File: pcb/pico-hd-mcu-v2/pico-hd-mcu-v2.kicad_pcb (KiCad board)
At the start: 2 copper layers, 87.9 x 88 mm, 43 parts

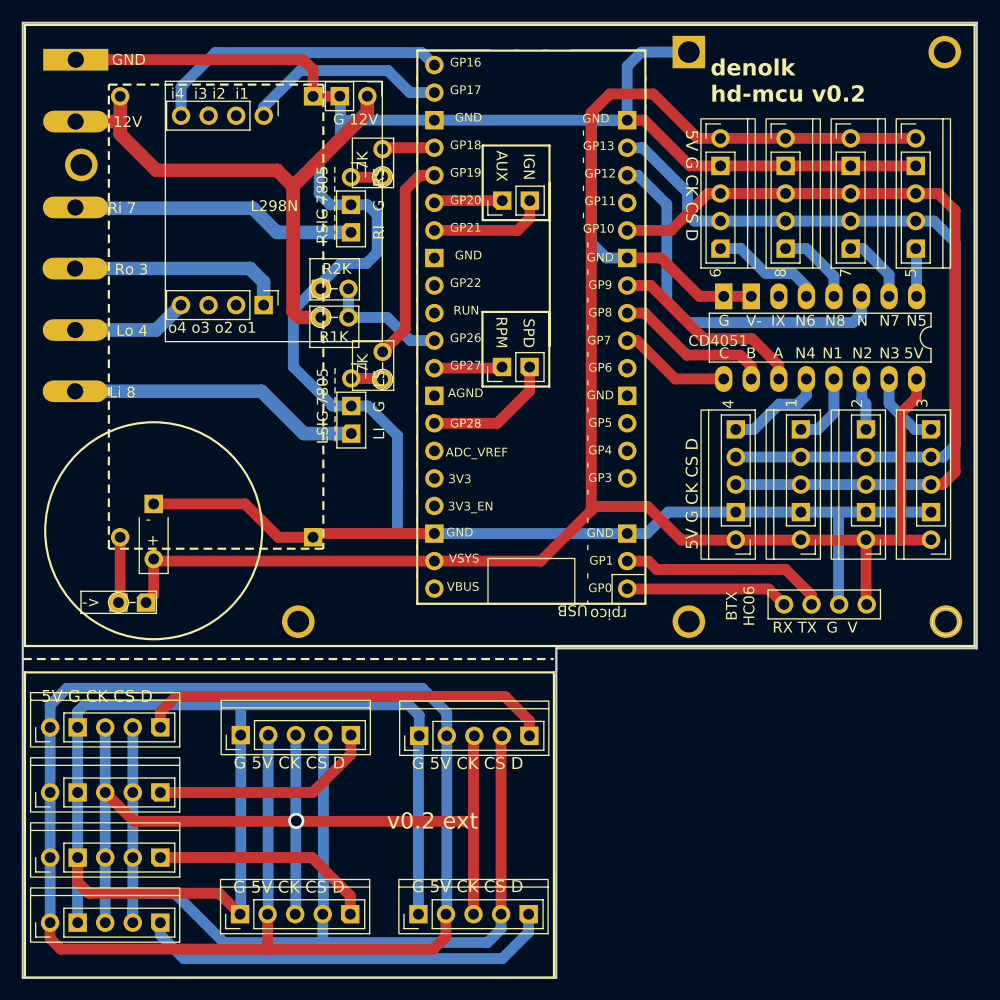
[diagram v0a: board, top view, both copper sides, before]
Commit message: update pcb - ext mosfet switch
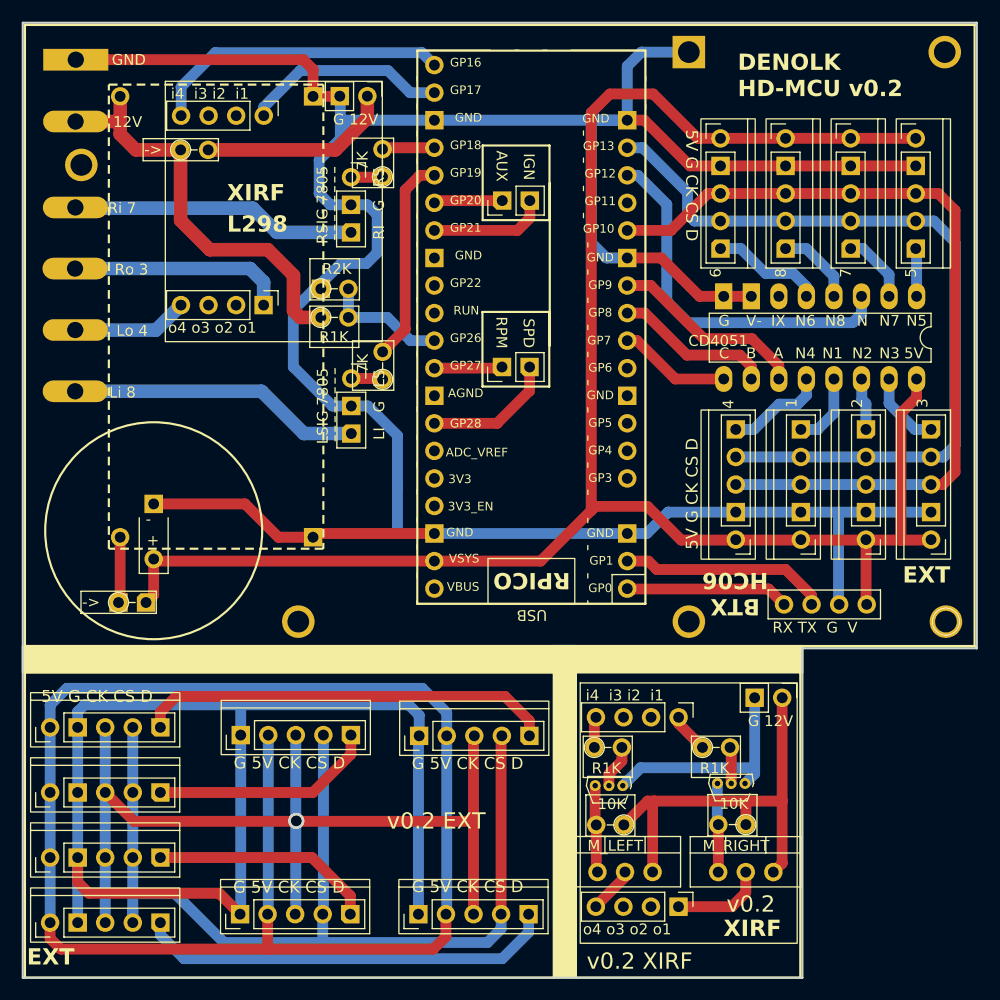
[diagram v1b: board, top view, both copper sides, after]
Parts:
- added ->: R_Axial_DIN0204_L3.6mm_D1.6mm_P2.54mm_Vertical, Resistor_THT:R_Axial_DIN0204_L3.6mm_D1.6mm_P2.54mm_Vertical, F.Cu at (36.4, 38.3)
- added 10K: R_Axial_DIN0204_L3.6mm_D1.6mm_P2.54mm_Vertical, Resistor_THT:R_Axial_DIN0204_L3.6mm_D1.6mm_P2.54mm_Vertical, F.Cu at (77.2, 100.5)
- added 10K: R_Axial_DIN0204_L3.6mm_D1.6mm_P2.54mm_Vertical, Resistor_THT:R_Axial_DIN0204_L3.6mm_D1.6mm_P2.54mm_Vertical, F.Cu at (88.5, 100.5)
- added R1K: R_Axial_DIN0204_L3.6mm_D1.6mm_P2.54mm_Vertical, Resistor_THT:R_Axial_DIN0204_L3.6mm_D1.6mm_P2.54mm_Vertical, F.Cu at (74.5, 93.4)
- added R1K: R_Axial_DIN0204_L3.6mm_D1.6mm_P2.54mm_Vertical, Resistor_THT:R_Axial_DIN0204_L3.6mm_D1.6mm_P2.54mm_Vertical, F.Cu at (84.5, 93.4)
- added REF**: 22RG, Package_TO_SOT_THT:TO-92S, F.Cu at (88.4, 96.7)
- added REF**: M_RIGHT, Package_TO_SOT_THT:TO-220-3_Vertical, F.Cu at (85.9, 104.9)
- added REF**: M_LEFT, Package_TO_SOT_THT:TO-220-3_Vertical, F.Cu at (74.8, 104.9)
- added REF**: L298N, denolk:L298N Motor driver board, F.Cu at (83.2, 97.9)
- added REF**: 22LF, Package_TO_SOT_THT:TO-92S, F.Cu at (77.1, 96.9)
- REF**: value L298N -> L298
- REF**: value rpico -> RPICO
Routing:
- net (no net): track 0.00 -> 104.8 mm
- net 12V: track 51.6 -> 56.8 mm
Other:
- outline, holes or cut-outs redrawn
- board text added: "12V REG"
- board text added: "DENOLK HD-MCU v0.2"
- board text added: "XIRF"
- board text added: "v0.2"
- board text added: "v0.2 EXT"
- board text added: "v0.2 XIRF"
- board text removed: "denolk hd-mcu v0.2"
- board text removed: "v0.2 ext"

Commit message: update pcb
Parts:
- REF**: value M_RIGHT -> MF_R
- REF**: value M_LEFT -> MF_L
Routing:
- net D_SIG_R_OUT: track 18.8 -> 20.1 mm
- net D_SIG_L_OUT: track 27.8 -> 28.6 mm
- net GND: track 271.3 -> 270.8 mm
